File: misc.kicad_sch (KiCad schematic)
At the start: 8 parts, among them J5 Board_1, U19 RIC11-31S10K2-GSMT

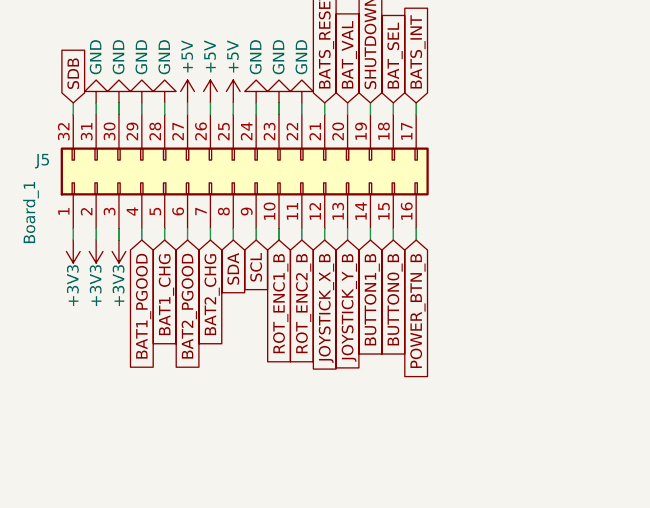
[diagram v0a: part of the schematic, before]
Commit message: Routed power section in the layout
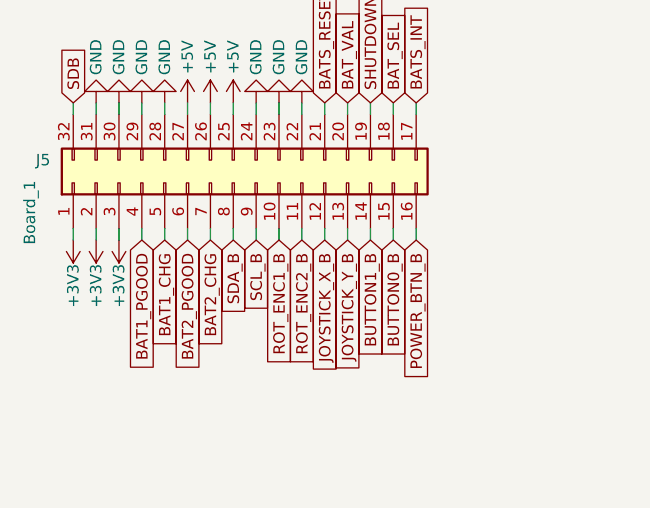
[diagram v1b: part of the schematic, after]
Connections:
- net SCL renamed SCL_B
- net SDA renamed SDA_B
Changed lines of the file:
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@@
 		)
 	)
-	(global_label "SCL"
+	(global_label "SCL_B"
 		(shape input)
 		(at 45.72 90.17 270)
@@
 		)
 		(property "Intersheetrefs" "${INTERSHEET_REFS}"
-			(at 45.72 96.6628 90)
+			(at 45.72 98.9004 90)
 			(hide yes)
 			(show_name no)
@@
 		)
 	)
-	(global_label "SDA"
+	(global_label "SDA_B"
 		(shape input)
 		(at 43.18 90.17 270)
@@
 		)
 		(property "Intersheetrefs" "${INTERSHEET_REFS}"
-			(at 43.18 96.7233 90)
+			(at 43.18 98.9609 90)
 			(hide yes)
 			(show_name no)

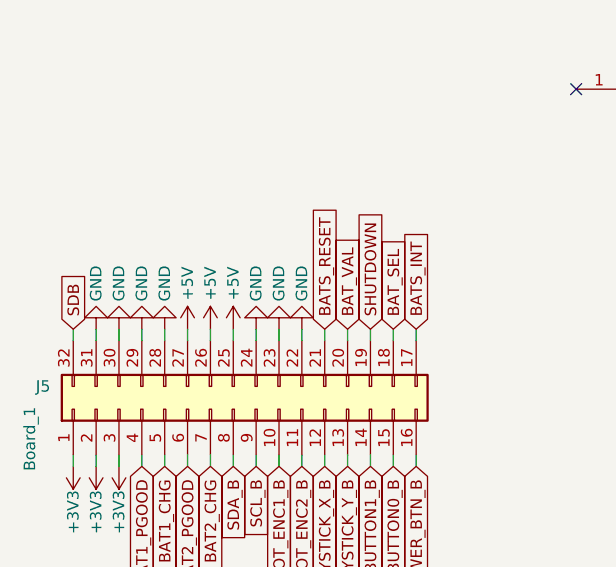
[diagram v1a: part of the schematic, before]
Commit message: Finished routing main PCB
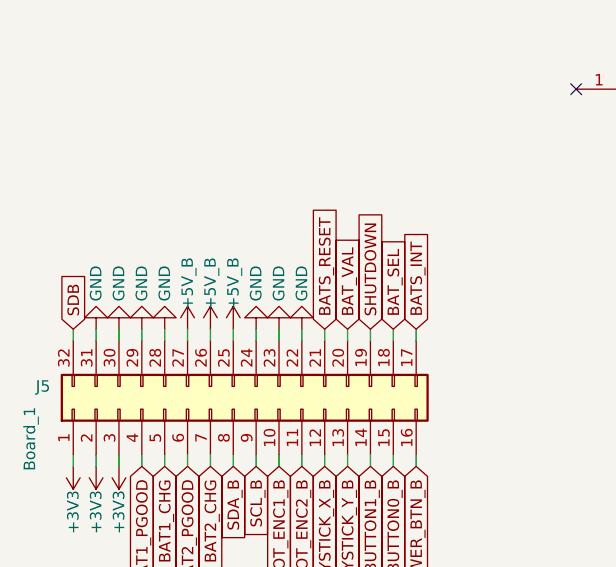
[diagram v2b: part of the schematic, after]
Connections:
- net +5V renamed +5V_B

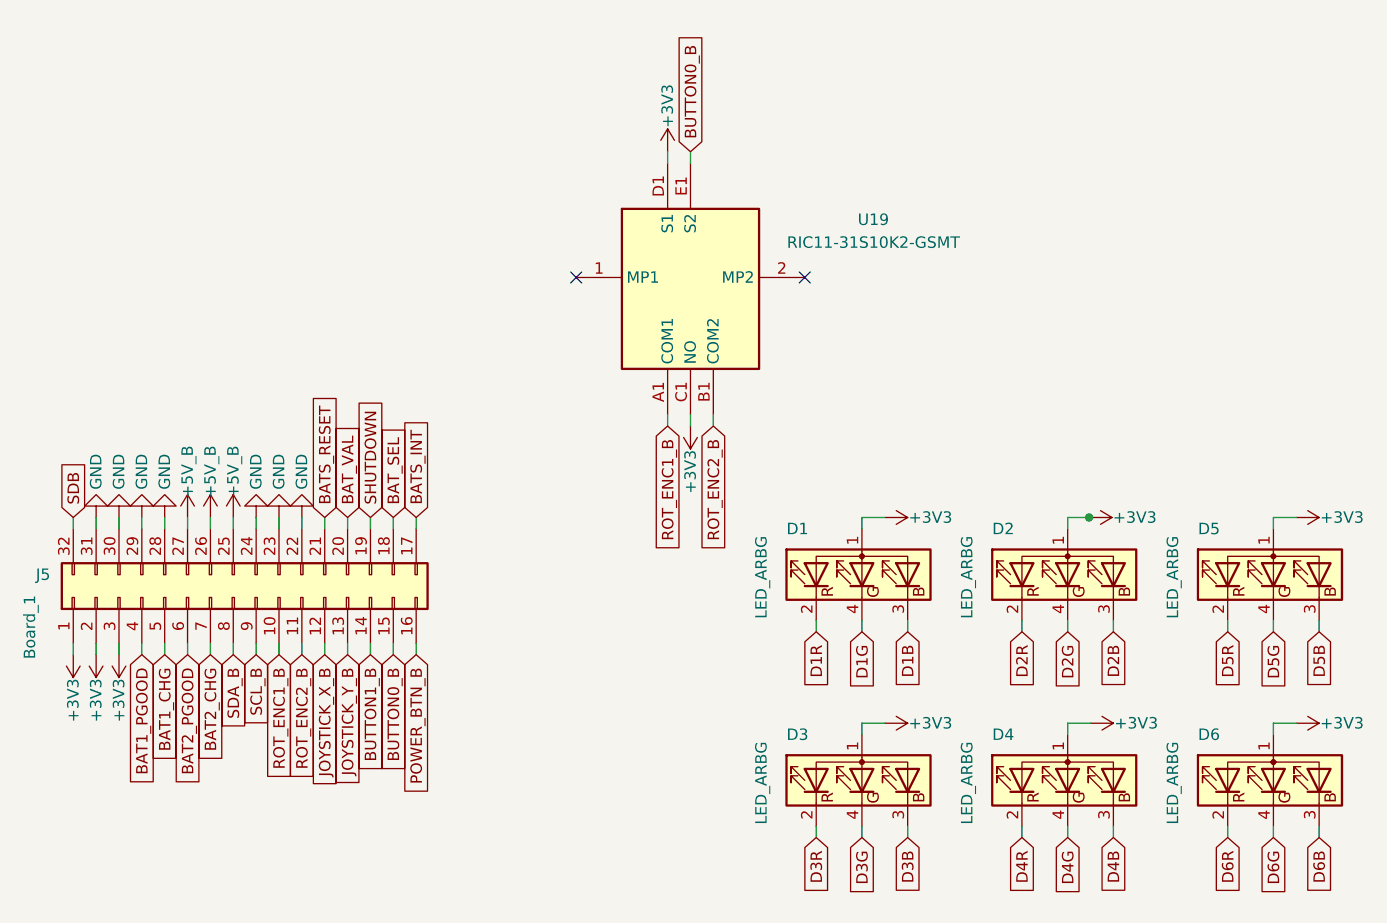
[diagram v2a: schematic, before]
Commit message: Routed all PCB, missing antenna variable capacitors
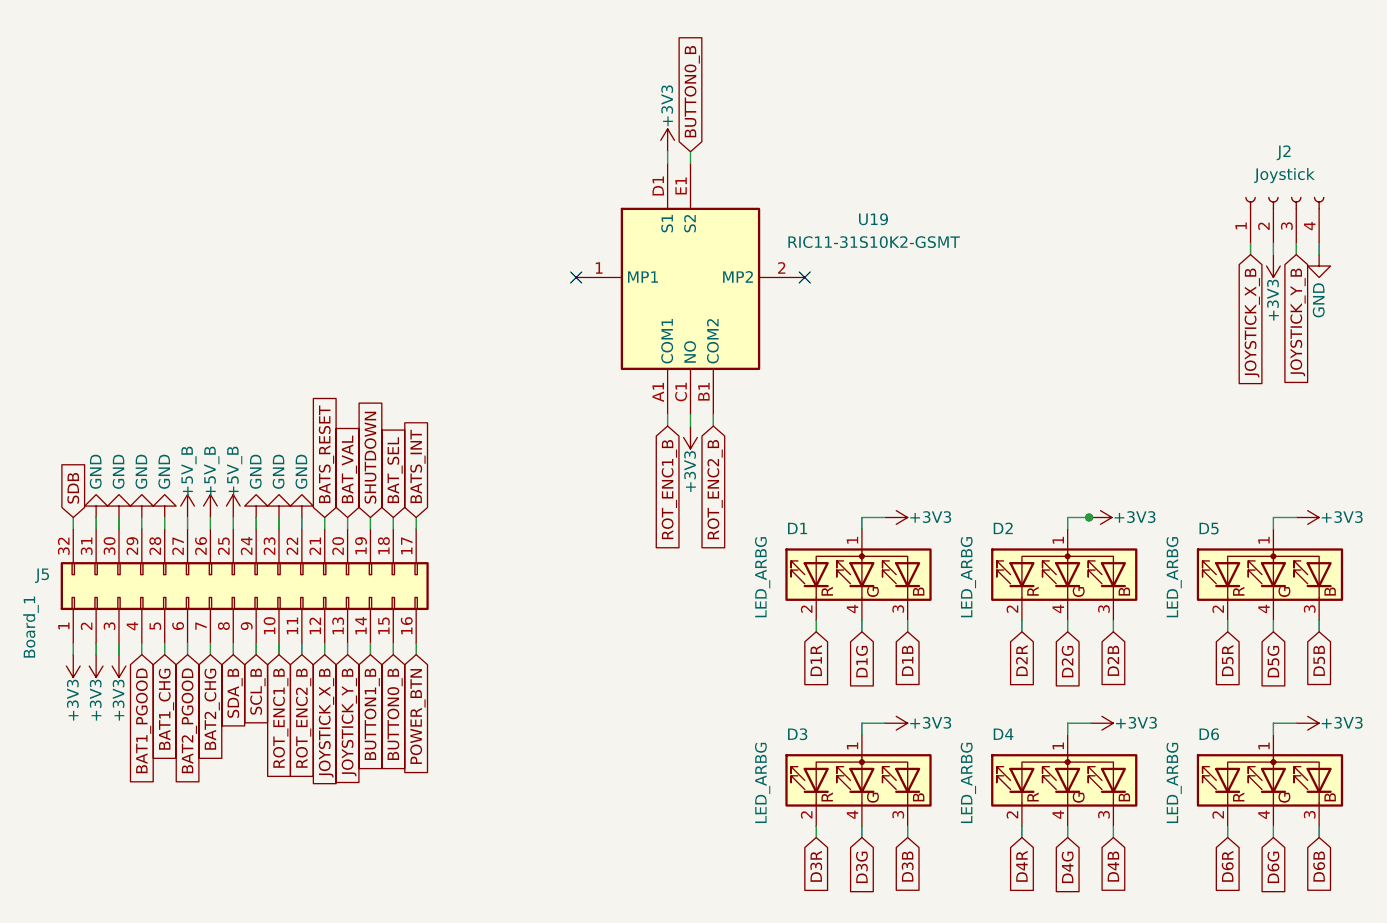
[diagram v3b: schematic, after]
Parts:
- added J2: Joystick, Connector_FFC-FPC:Amphenol_F32Q-1A7x1-11004_1x04-1MP_P0.5mm_Horizontal, symbol Connector:Conn_01x04_Socket
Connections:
- net +3V3: now also J2.2 (Pin_2)
- net GND: now also J2.4 (Pin_4)
- net JOYSTICK_X_B: now also J2.1 (Pin_1)
- net JOYSTICK_Y_B: now also J2.3 (Pin_3)
- net POWER_BTN_B renamed POWER_BTN

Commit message: Finishing routing unrouted nets and verifying DRC
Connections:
- net +5V_B renamed BAT_OUT
